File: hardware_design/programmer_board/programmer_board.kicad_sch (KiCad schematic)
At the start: 4 parts, among them J1 USB4800-03-A_REVA, U1 CH340G

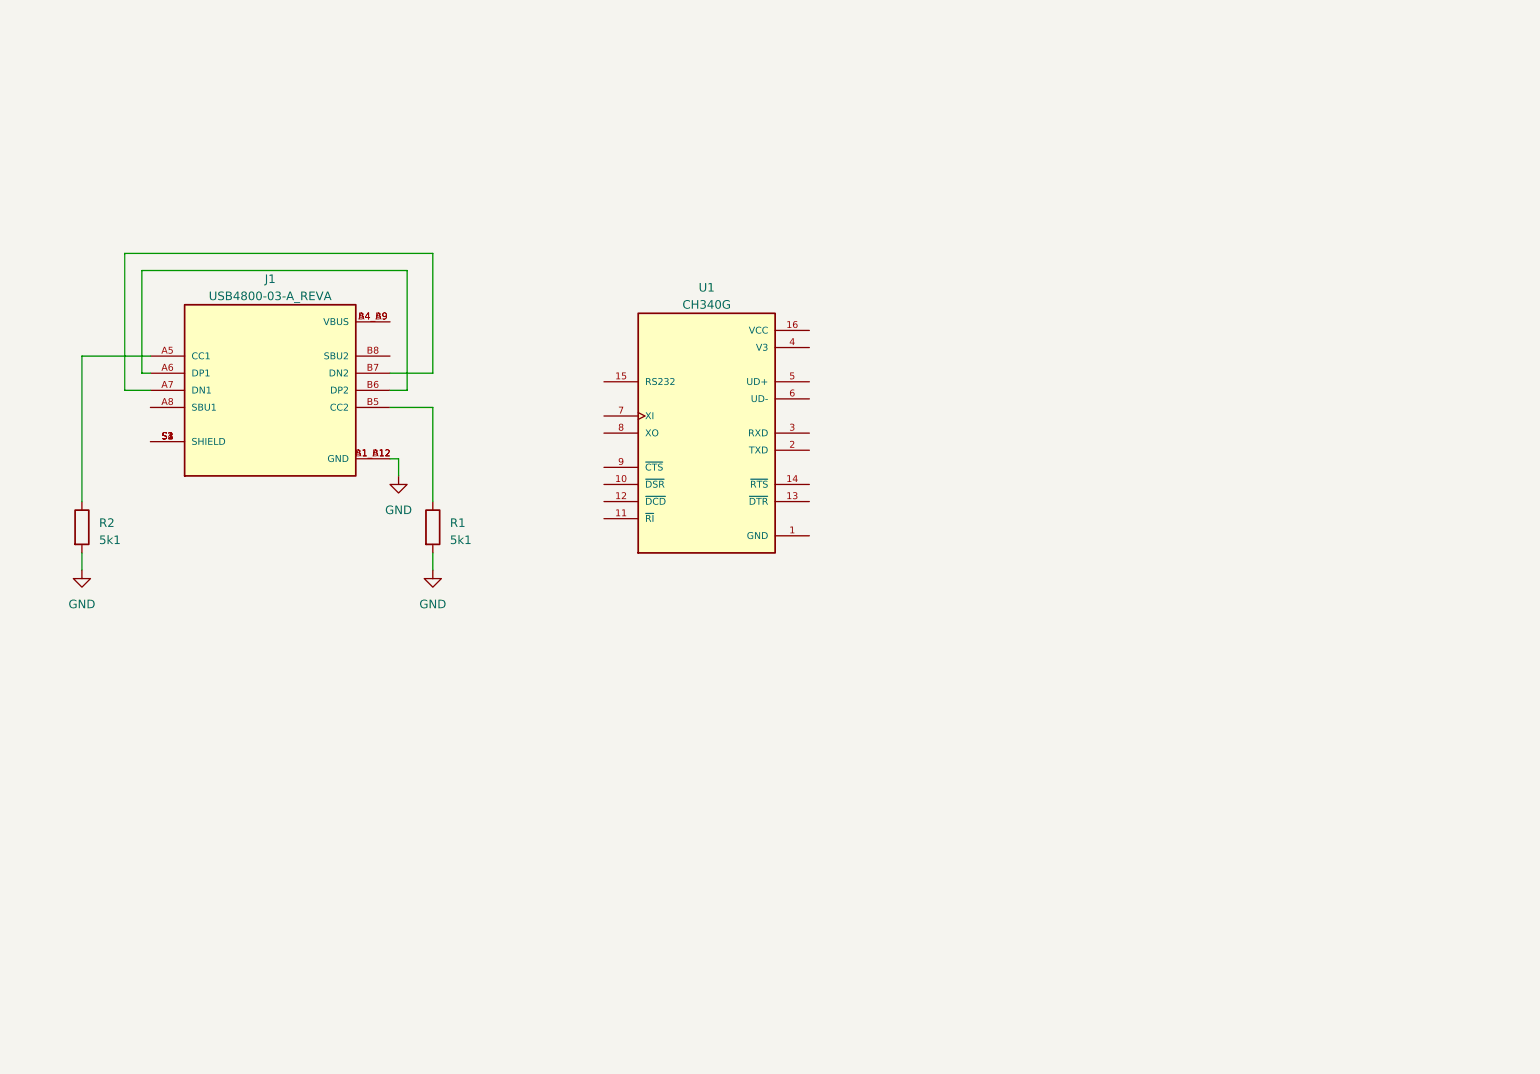
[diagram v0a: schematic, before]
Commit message: Updated programmer schematic
Started development on programmer schematic
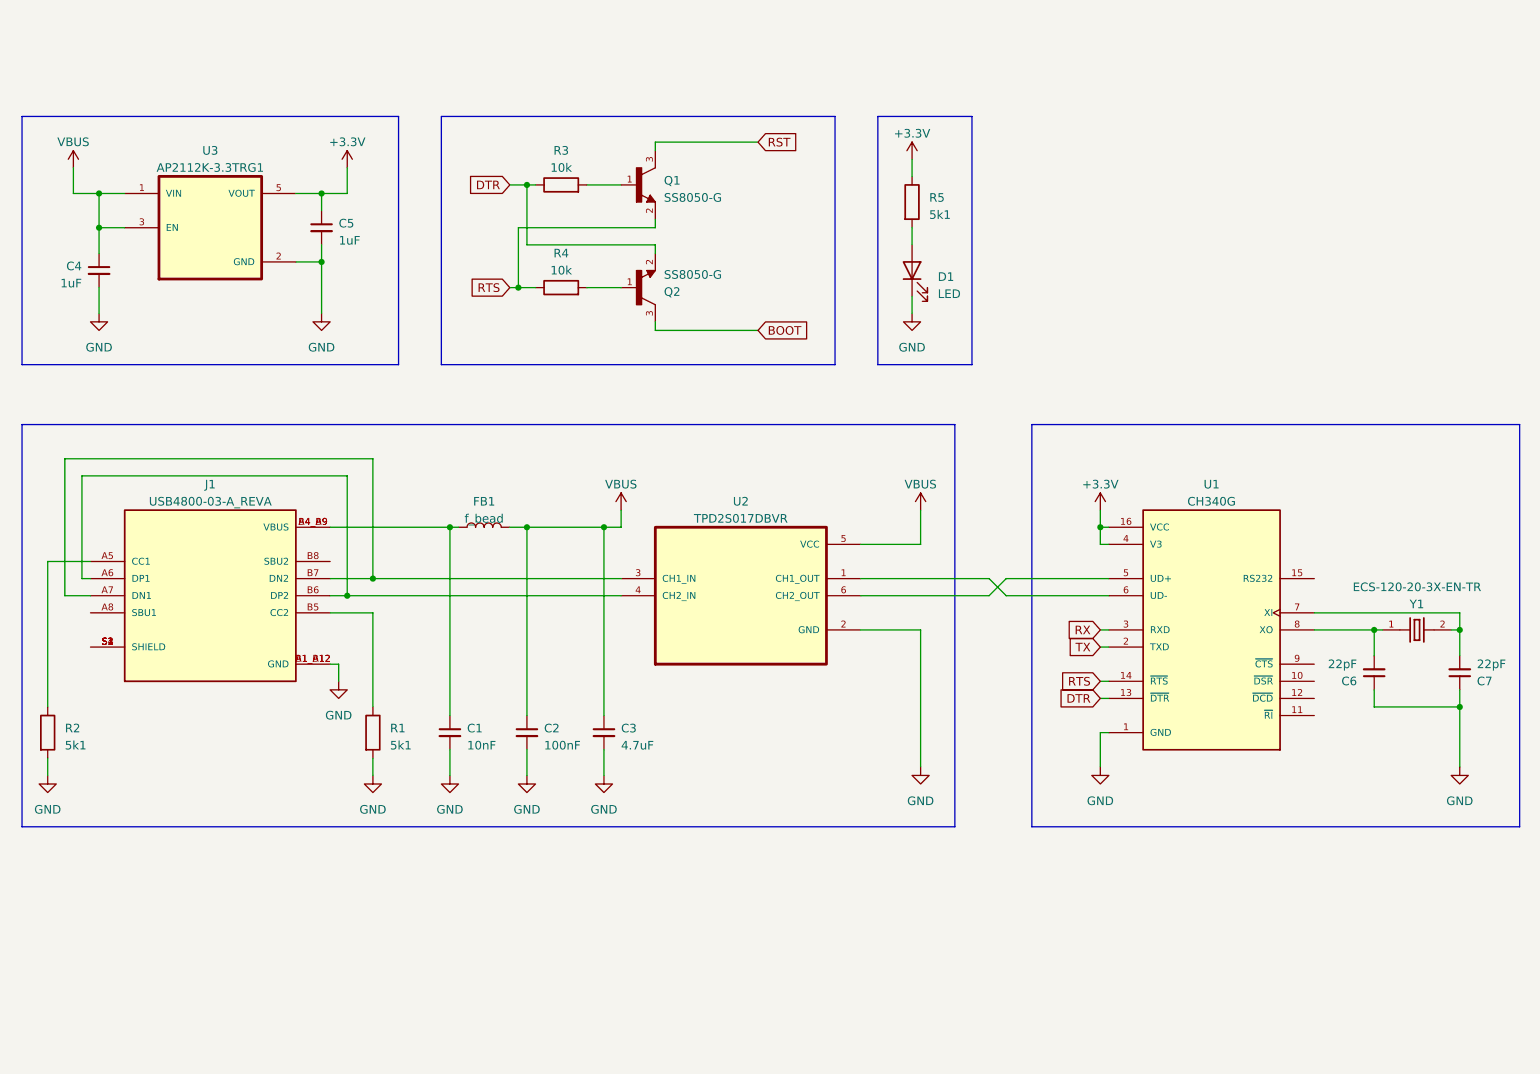
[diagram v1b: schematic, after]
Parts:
- added C1: 10nF, Capacitor_SMD:C_0603_1608Metric, symbol Device:C_Small
- added C2: 100nF, Capacitor_SMD:C_0603_1608Metric, symbol Device:C_Small
- added C3: 4.7uF, Capacitor_SMD:C_0603_1608Metric, symbol Device:C_Small
- added C4, C5: 1uF, Capacitor_SMD:C_0603_1608Metric, symbol Device:C_Small
- added C6, C7: 22pF, Capacitor_SMD:C_0603_1608Metric, symbol Device:C_Small
- added D1: LED, Diode_SMD:D_0603_1608Metric, symbol Device:LED
- added FB1: f_bead, Inductor_SMD:L_0805_2012Metric, symbol Device:L
- added Q1, Q2: SS8050-G, TRANS_SS8050-G, symbol SS8050-G:SS8050-G
- added R3, R4: 10k, Resistor_SMD:R_0603_1608Metric, symbol Device:R
- added R5: 5k1, Resistor_SMD:R_0603_1608Metric, symbol Device:R
- added U2: TPD2S017DBVR, SOT95P280X145-6N, symbol TPD2S017DBVR:TPD2S017DBVR
- added U3: AP2112K-3.3TRG1, SOT95P285X140-5N, symbol AP2112K-3.3TRG1:AP2112K-3.3TRG1
- added Y1: ECS-120-20-3X-EN-TR, XTAL_ECS-120-20-3X-EN-TR, symbol ECS-120-20-3X-EN-TR:ECS-120-20-3X-EN-TR
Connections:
- net GND: now also U1.1 (GND), C1.2, C2.2, C3.2, C4.2, C5.2, C6.1, C7.1, D1.1 (K), U2.2 (GND), U3.2 (GND)
- net at J1.A4_B9 (VBUS), J1.B4_A9 (VBUS): now also C1.1, FB1.1
- net at J1.A6 (DP1), J1.B6 (DP2): now also U2.4 (CH2_IN)
- net at J1.A7 (DN1), J1.B7 (DN2): now also U2.3 (CH1_IN)
- net DTR: now reaches U1.13 (~{DTR})
- net DTR: now also Q2.2, R3.1
- net RTS: now reaches U1.14 (~{RTS})
- net RTS: now also Q1.2, R4.1
- net +3.3V: now reaches U1.16 (VCC)
- net +3.3V: now also U1.4 (V3), C5.1, R5.1, U3.5 (VOUT)
- net TX: now reaches U1.2 (TXD)
- net RX: now reaches U1.3 (RXD)
- net at U1.5 (UD+): now also U2.6 (CH2_OUT)
- net at U1.6 (UD-): now also U2.1 (CH1_OUT)
- net at U1.7 (XI): now also C7.2, Y1.2
- net at U1.8 (XO): now also C6.2, Y1.1
- new net: Q1.1, R3.2
- new net: D1.2 (A), R5.2
- new net: Q2.1, R4.2
- new net BOOT: Q2.3
- new net RST: Q1.3
- new net VBUS: C2.1, C3.1, C4.1, FB1.2, U2.5 (VCC), U3.1 (VIN), U3.3 (EN)
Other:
- moved on the sheet: J1, R1, R2, U1

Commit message: Finished programmer schematic
Programmer schematic drawn. Review.
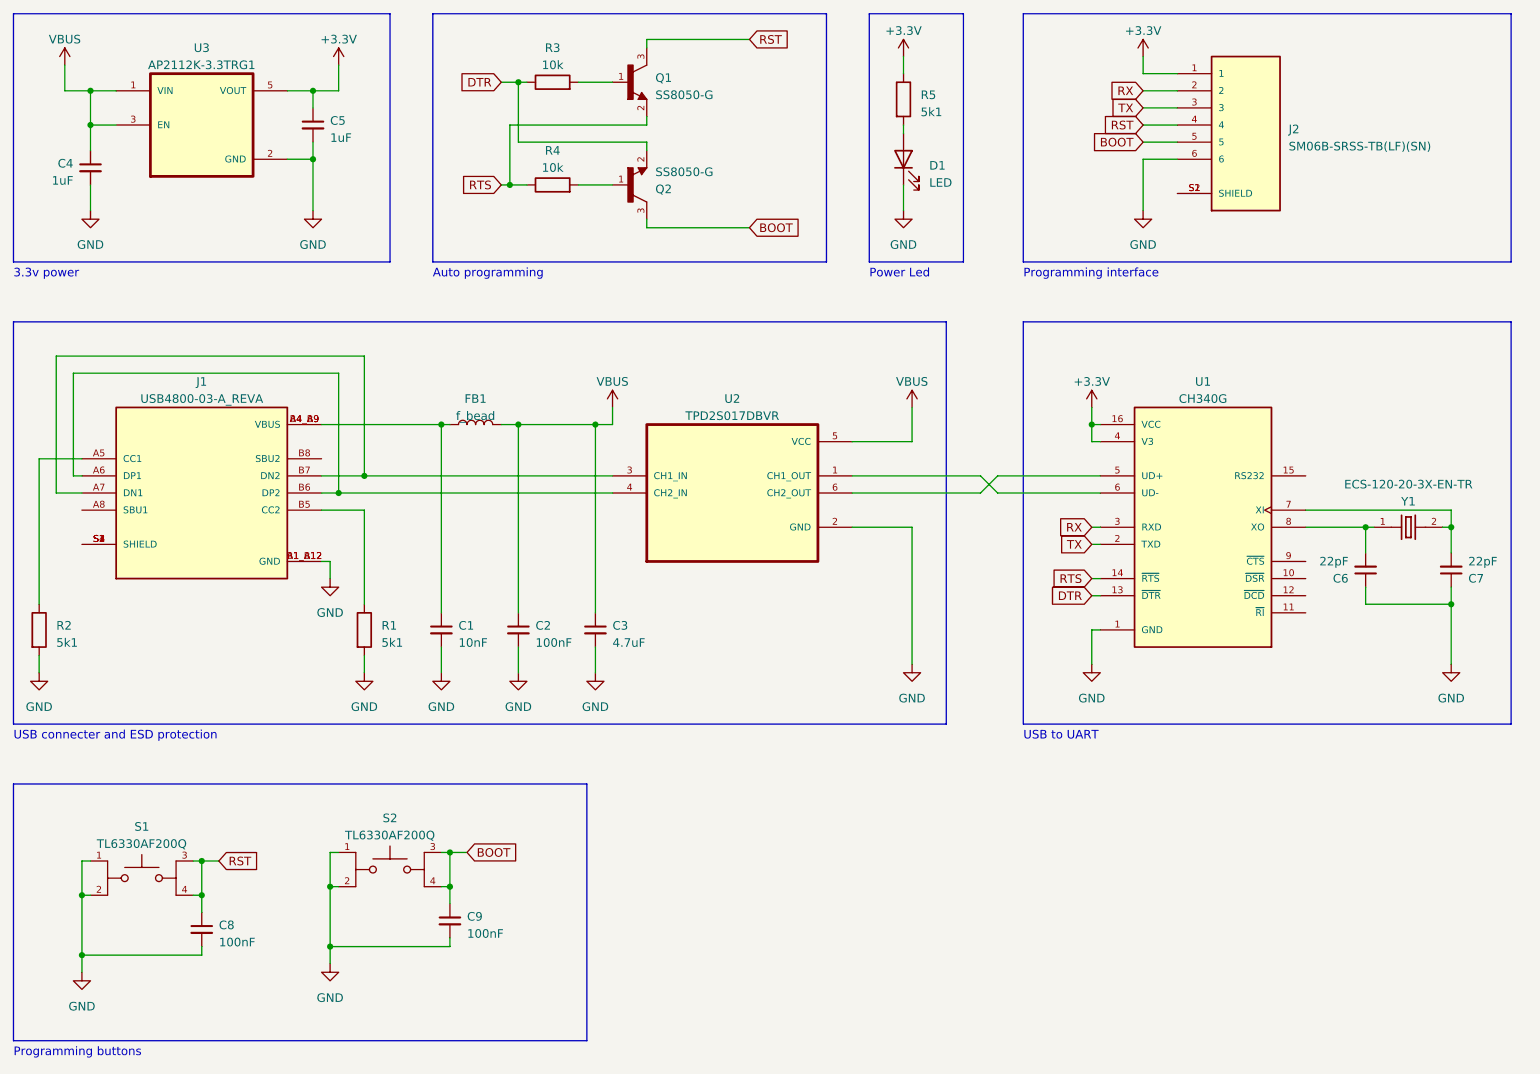
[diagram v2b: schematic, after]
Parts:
- added C8, C9: 100nF, Capacitor_SMD:C_0603_1608Metric, symbol Device:C_Small
- added J2: SM06B-SRSS-TB(LF)(SN), JST_SM06B-SRSS-TB(LF)(SN), symbol SM06B-SRSS-TB_LF__SN_:SM06B-SRSS-TB(LF)(SN)
- added S1, S2: TL6330AF200Q, SW_TL6330AF200Q, symbol TL6330AF200Q:TL6330AF200Q
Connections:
- net +3.3V: now also J2.1
- net BOOT: now also C9.1, J2.5, S2.3, S2.4
- net GND: now also C8.2, C9.2, J2.6, S1.1, S1.2, S2.1, S2.2
- net RST: now also C8.1, J2.4, S1.3, S1.4
- net RX: now also J2.2
- net TX: now also J2.3
- new net: J2.S1 (SHIELD), J2.S2 (SHIELD)
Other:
- note added: "3.3v power"
- note added: "Auto programming"
- note added: "Power Led"
- note added: "Programming buttons"
- note added: "Programming interface"
- note added: "USB connecter and ESD protection"
- note added: "USB to UART"
- title: (none) -> ESP board programmer
- moved on the sheet: C1, C2, C3, C4, C5, C6, C7, D1, FB1, J1, Q1, Q2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

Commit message: Started programmer pcb design
Started programmer PCB design
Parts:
- added R1: 0, Resistor_SMD:R_0603_1608Metric, symbol Device:R
- renumbered C5 to C1, C4 to C2, C6 to C3, C7 to C4, C1 to C5, C2 to C6, C3 to C7, C9 to C8, C8 to C9, J2 to J1, J1 to J2, R3 to R2, R5 to R3, R2 to R5, R1 to R6, S2 to S1, S1 to S2, U3 to U1, U1 to U3
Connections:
- net +3.3V: now also R1.1; no longer J1.1
- net USB_N: now reaches U2.1 (CH1_OUT), U3.6 (UD-)
- net USB_N: now also J2.A7 (DN1), J2.B7 (DN2), U2.3 (CH1_IN)
- net USB_P: now reaches J2.A6 (DP1), J2.B6 (DP2), U2.4 (CH2_IN)
- net USB_P: now also U2.6 (CH2_OUT), U3.5 (UD+)
- new net: J1.1, R1.2
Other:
- moved on the sheet: J1
